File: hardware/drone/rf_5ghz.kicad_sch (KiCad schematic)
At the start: 19 parts, among them J5 Conn_01x06_Pin, U7 CC3350, U8 DPX167125DT-8197B1, U9 DEA162450BT-1295A1, Y1 Crystal_GND24

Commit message: Small cleanup
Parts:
- added R35, R36, R37, R38, R39: R, symbol Device:R
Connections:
- net CC_SDMMC1_CMD: now also R35.2
- net CC_SDMMC1_D0: now also R36.2
- net CC_SDMMC1_D1: now also R37.2
- net CC_SDMMC1_D2: now also R38.2
- net CC_SDMMC1_D3: now also R39.2
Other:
- moved on the sheet: C43, C44, Y1

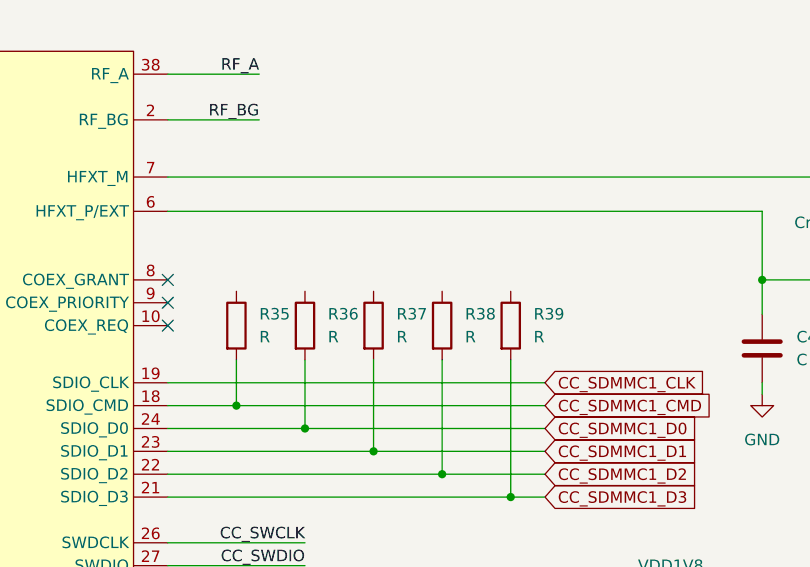
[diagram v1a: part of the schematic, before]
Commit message: Small cleanup and pinmuxxed OSPI_NRESET
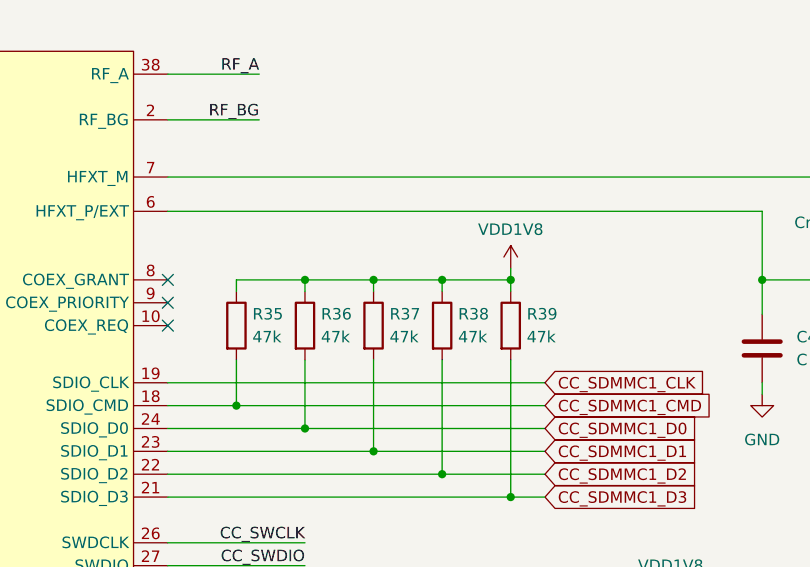
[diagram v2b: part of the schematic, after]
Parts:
- R35, R36, R37, R38, R39: value R -> 47k
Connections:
- net VDD1V8: now also R35.1, R36.1, R37.1, R38.1, R39.1
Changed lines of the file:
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@@
 	)
 	(junction
+		(at 166.37 62.23)
+		(diameter 0)
+		(color 0 0 0 0)
+	)
+	(junction
 		(at 53.34 165.1)
 		(diameter 0)
@@
 	)
 	(junction
+		(at 173.99 62.23)
+		(diameter 0)
+		(color 0 0 0 0)
+	)
+	(junction
+		(at 181.61 62.23)
+		(diameter 0)
+		(color 0 0 0 0)
+	)
+	(junction
+		(at 189.23 62.23)
+		(diameter 0)
+		(color 0 0 0 0)
+	)
+	(junction
 		(at 77.47 39.37)
 		(diameter 0)
@@
 	(wire
 		(pts
+			(xy 173.99 62.23) (xy 173.99 63.5)
+		)
+		(stroke
+			(width 0)
+			(type default)
+		)
+	)
+	(wire
+		(pts
 			(xy 62.23 74.93) (xy 62.23 76.2)
 		)
@@
 	(wire
 		(pts
+			(xy 189.23 62.23) (xy 189.23 60.96)
+		)
+		(stroke
+			(width 0)
+			(type default)
+		)
+	)
+	(wire
+		(pts
+			(xy 189.23 62.23) (xy 189.23 63.5)
+		)
+		(stroke
+			(width 0)
+			(type default)
+		)
+	)
+	(wire
+		(pts
 			(xy 207.01 99.06) (xy 207.01 101.6)
 		)
@@
 	(wire
 		(pts
+			(xy 173.99 62.23) (xy 181.61 62.23)
+		)
+		(stroke
+			(width 0)
+			(type default)
+		)
+	)
+	(wire
+		(pts
+			(xy 158.75 62.23) (xy 166.37 62.23)
+		)
+		(stroke
+			(width 0)
+			(type default)
+		)
+	)
+	(wire
+		(pts
 			(xy 90.17 64.77) (xy 81.28 64.77)
 		)
@@
 	(wire
 		(pts
+			(xy 181.61 62.23) (xy 189.23 62.23)
+		)
+		(stroke
+			(width 0)
+			(type default)
+		)
+	)
+	(wire
+		(pts
 			(xy 110.49 165.1) (xy 114.3 165.1)
 		)
@@
 	(wire
 		(pts
+			(xy 158.75 63.5) (xy 158.75 62.23)
+		)
+		(stroke
+			(width 0)
+			(type default)
+		)
+	)
+	(wire
+		(pts
 			(xy 151.13 86.36) (xy 189.23 86.36)
 		)
@@
 	(wire
 		(pts
+			(xy 166.37 62.23) (xy 173.99 62.23)
+		)
+		(stroke
+			(width 0)
+			(type default)
+		)
+	)
+	(wire
+		(pts
 			(xy 86.36 139.7) (xy 88.9 139.7)
 		)
@@
 	(wire
 		(pts
+			(xy 181.61 62.23) (xy 181.61 63.5)
+		)
+		(stroke
+			(width 0)
+			(type default)
+		)
+	)
+	(wire
+		(pts
 			(xy 237.49 73.66) (xy 237.49 74.93)
 		)
@@
 	(wire
 		(pts
+			(xy 166.37 62.23) (xy 166.37 63.5)
+		)
+		(stroke
+			(width 0)
+			(type default)
+		)
+	)
+	(wire
+		(pts
 			(xy 196.85 106.68) (xy 209.55 106.68)
 		)
@@
 		(in_pos_files yes)
 		(dnp no)
-		(fields_autoplaced yes)
 		(property "Reference" "R35"
-			(at 161.29 66.0399 0)
+			(at 160.528 66.04 0)
 			(show_name no)
 			(do_not_autoplace no)
@@
 			)
 		)
-		(property "Value" "R"
-			(at 161.29 68.5799 0)
+		(property "Value" "47k"
+			(at 160.528 68.58 0)
 			(show_name no)
 			(do_not_autoplace no)
@@
 		(in_pos_files yes)
 		(dnp no)
-		(fields_autoplaced yes)
 		(property "Reference" "R38"
-			(at 184.15 66.0399 0)
+			(at 183.388 66.04 0)
 			(show_name no)
 			(do_not_autoplace no)
@@
 			)
 		)
-		(property "Value" "R"
-			(at 184.15 68.5799 0)
+		(property "Value" "47k"
+			(at 183.388 68.58 0)
 			(show_name no)
 			(do_not_autoplace no)
@@
 		(in_pos_files yes)
 		(dnp no)
-		(fields_autoplaced yes)
 		(property "Reference" "R36"
-			(at 168.91 66.0399 0)
+			(at 168.148 66.04 0)
 			(show_name no)
 			(do_not_autoplace no)
@@
 			)
 		)
-		(property "Value" "R"
-			(at 168.91 68.5799 0)
+		(property "Value" "47k"
+			(at 168.148 68.58 0)
 			(show_name no)
 			(do_not_autoplace no)
@@
 		(in_pos_files yes)
 		(dnp no)
-		(fields_autoplaced yes)
 		(property "Reference" "R39"
-			(at 191.77 66.0399 0)
+			(at 191.008 66.04 0)
 			(show_name no)
 			(do_not_autoplace no)
@@
 			)
 		)
-		(property "Value" "R"
-			(at 191.77 68.5799 0)
+		(property "Value" "47k"
+			(at 191.008 68.58 0)
 			(show_name no)
 			(do_not_autoplace no)
@@
 	)
 	(symbol
+		(lib_id "power:VDD")
+		(at 189.23 60.96 0)
+		(unit 1)
+		(body_style 1)
+		(exclude_from_sim no)
+		(in_bom yes)
+		(on_board yes)
+		(in_pos_files yes)
+		(dnp no)
+		(property "Reference" "#PWR0196"
+			(at 189.23 64.77 0)
+			(hide yes)
+			(show_name no)
+			(do_not_autoplace no)
+			(effects
+				(font
+					(size 1.27 1.27)
+				)
+			)
+		)
+		(property "Value" "VDD1V8"
+			(at 189.23 56.642 0)
+			(show_name no)
+			(do_not_autoplace no)
+			(effects
+				(font
+					(size 1.27 1.27)
+				)
+			)
+		)
+		(property "Footprint" ""
+			(at 189.23 60.96 0)
+			(hide yes)
+			(show_name no)
+			(do_not_autoplace no)
+			(effects
+				(font
+					(size 1.27 1.27)
+				)
+			)
+		)
+		(property "Datasheet" ""
+			(at 189.23 60.96 0)
+			(hide yes)
+			(show_name no)
+			(do_not_autoplace no)
+			(effects
+				(font
+					(size 1.27 1.27)
+				)
+			)
+		)
+		(property "Description" "Power symbol creates a global label with name \"VDD\""
+			(at 189.23 60.96 0)
+			(hide yes)
+			(show_name no)
+			(do_not_autoplace no)
+			(effects
+				(font
+					(size 1.27 1.27)
+				)
+			)
+		)
+		(pin "1"
+		)
+		(instances
+			(project "drone"
+				(path "/62c402a6-ed3f-446b-8423-821e9cc6908b/5e69e925-338b-411d-9923-3dc150eb85e3"
+					(reference "#PWR0196")
+					(unit 1)
+				)
+			)
+		)
+	)
+	(symbol
 		(lib_id "Device:R")
 		(at 173.99 67.31 0)
@@
 		(in_pos_files yes)
 		(dnp no)
-		(fields_autoplaced yes)
 		(property "Reference" "R37"
-			(at 176.53 66.0399 0)
+			(at 175.768 66.04 0)
 			(show_name no)
 			(do_not_autoplace no)
@@
 			)
 		)
-		(property "Value" "R"
-			(at 176.53 68.5799 0)
+		(property "Value" "47k"
+			(at 175.768 68.58 0)
 			(show_name no)
 			(do_not_autoplace no)

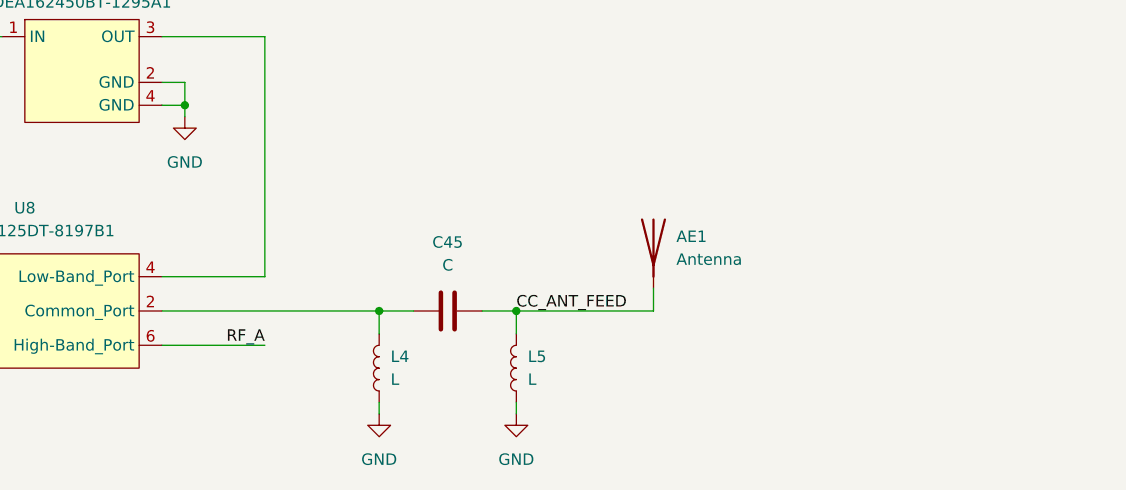
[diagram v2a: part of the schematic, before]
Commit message: Added easier RF tuning setup with MM8030
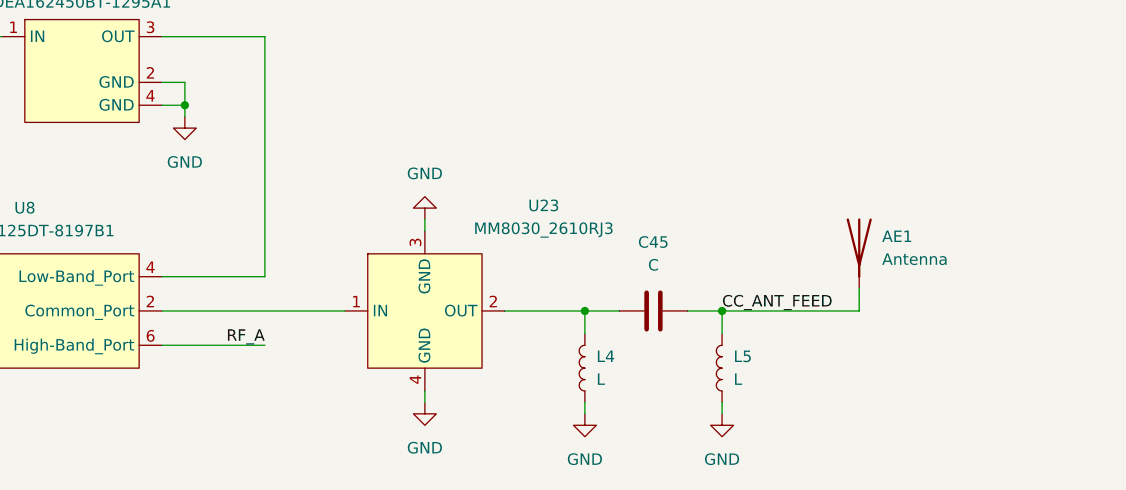
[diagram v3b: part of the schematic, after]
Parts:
- added U23: MM8030_2610RJ3, symbol SoftDrone:MM8030_2610RJ3
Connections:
- net GND: now also U23.3 (GND), U23.4 (GND)
- net at C45.1, L4.2: now also U23.2 (OUT); no longer U8.2 (Common_Port)
- new net: U23.1 (IN), U8.2 (Common_Port)
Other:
- moved on the sheet: AE1, C45, L4, L5

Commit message: Started footprint assignments
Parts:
- J5: footprint RF_Module:Ai-Thinker-Ra-01-LoRa -> (none)
- U7: footprint Display_7Segment:CC56-12GWA -> CC3350ENJARSBR:QFN40P500X500X80-41N-D
- U8: footprint (none) -> DPX167125DT-8197B1:DPX167125DT8197B1
- U9: footprint (none) -> DEA162450BT-1295A1:DEA162450BT1295A1
- Y1: footprint Package_DFN_QFN:DFN-6-1EP_3x2mm_P0.5mm_EP1.65x1.35mm -> (none)
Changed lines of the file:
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@@
 			)
 		)
-		(property "Footprint" ""
+		(property "Footprint" "DEA162450BT-1295A1:DEA162450BT1295A1"
 			(at 77.47 138.43 0)
 			(hide yes)
@@
 			)
 		)
-		(property "Footprint" ""
+		(property "Footprint" "DPX167125DT-8197B1:DPX167125DT8197B1"
 			(at 71.12 165.1 0)
 			(hide yes)
@@
 			)
 		)
-		(property "Footprint" "RF_Module:Ai-Thinker-Ra-01-LoRa"
+		(property "Footprint" ""
 			(at 214.63 106.68 0)
 			(hide yes)
@@
 			)
 		)
-		(property "Footprint" "Display_7Segment:CC56-12GWA"
+		(property "Footprint" "CC3350ENJARSBR:QFN40P500X500X80-41N-D"
 			(at 120.65 73.66 0)
 			(hide yes)
@@
 			)
 		)
-		(property "Footprint" "Package_DFN_QFN:DFN-6-1EP_3x2mm_P0.5mm_EP1.65x1.35mm"
+		(property "Footprint" ""
 			(at 227.33 62.23 0)
 			(hide yes)

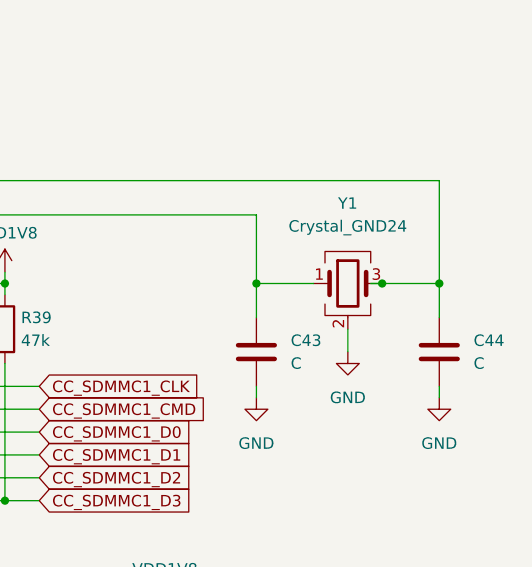
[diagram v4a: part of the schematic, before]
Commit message: Continued footprint assignments
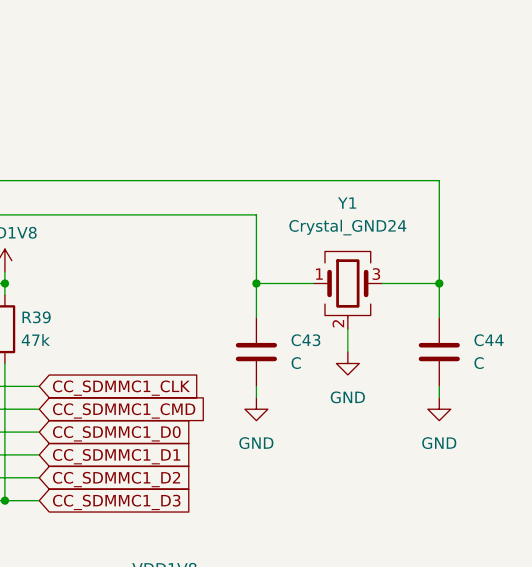
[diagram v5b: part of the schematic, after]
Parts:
- U23: footprint (none) -> SoftDroneLibrary:MM8030-2610RJ3
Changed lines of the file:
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@@
+	)
+	(junction
+		(at 237.49 62.23)
+		(diameter 0)
+		(color 0 0 0 0)
 	)
 	(junction
@@
 	)
 	(junction
-		(at 237.49 62.23)
-		(diameter 0)
-		(color 0 0 0 0)
-	)
-	(junction
 		(at 123.19 115.57)
 		(diameter 0)
@@
 	(junction
 		(at 217.17 62.23)
-		(diameter 0)
-		(color 0 0 0 0)
-	)
-	(junction
-		(at 231.14 62.23)
 		(diameter 0)
 		(color 0 0 0 0)
@@
 	(wire
 		(pts
-			(xy 229.87 62.23) (xy 231.14 62.23)
-		)
-		(stroke
-			(width 0)
-			(type default)
-		)
-	)
-	(wire
-		(pts
 			(xy 87.63 46.99) (xy 87.63 44.45)
 		)
@@
 	(wire
 		(pts
-			(xy 237.49 62.23) (xy 231.14 62.23)
-		)
-		(stroke
-			(width 0)
-			(type default)
-		)
-	)
-	(wire
-		(pts
 			(xy 90.17 57.15) (xy 87.63 57.15)
 		)
@@
 	(wire
 		(pts
+			(xy 231.14 62.23) (xy 237.49 62.23)
+		)
+		(stroke
+			(width 0)
+			(type default)
+		)
+	)
+	(wire
+		(pts
 			(xy 148.59 165.1) (xy 163.83 165.1)
 		)
@@
 	(wire
 		(pts
+			(xy 133.35 165.1) (xy 133.35 167.64)
+		)
+		(stroke
+			(width 0)
+			(type default)
+		)
+	)
+	(wire
+		(pts
+			(xy 166.37 62.23) (xy 166.37 63.5)
+		)
+		(stroke
+			(width 0)
+			(type default)
+		)
+	)
+	(wire
+		(pts
+			(xy 196.85 106.68) (xy 209.55 106.68)
+		)
+		(stroke
+			(width 0)
+			(type default)
+		)
+	)
+	(wire
+		(pts
+			(xy 31.75 48.26) (xy 31.75 49.53)
+		)
+		(stroke
+			(width 0)
+			(type default)
+		)
+	)
+	(wire
+		(pts
+			(xy 86.36 165.1) (xy 106.68 165.1)
+		)
+		(stroke
+			(width 0)
+			(type default)
+		)
+	)
+	(wire
+		(pts
+			(xy 40.64 62.23) (xy 81.28 62.23)
+		)
+		(stroke
+			(width 0)
+			(type default)
+		)
+	)
+	(wire
+		(pts
+			(xy 97.79 161.29) (xy 86.36 161.29)
+		)
+		(stroke
+			(width 0)
+			(type default)
+		)
+	)
+	(wire
+		(pts
+			(xy 148.59 165.1) (xy 144.78 165.1)
+		)
+		(stroke
+			(width 0)
+			(type default)
+		)
+	)
+	(wire
+		(pts
 			(xy 237.49 62.23) (xy 237.49 66.04)
-		)
-		(stroke
-			(width 0)
-			(type default)
-		)
-	)
-	(wire
-		(pts
-			(xy 133.35 165.1) (xy 133.35 167.64)
-		)
-		(stroke
-			(width 0)
-			(type default)
-		)
-	)
-	(wire
-		(pts
-			(xy 166.37 62.23) (xy 166.37 63.5)
-		)
-		(stroke
-			(width 0)
-			(type default)
-		)
-	)
-	(wire
-		(pts
-			(xy 196.85 106.68) (xy 209.55 106.68)
-		)
-		(stroke
-			(width 0)
-			(type default)
-		)
-	)
-	(wire
-		(pts
-			(xy 31.75 48.26) (xy 31.75 49.53)
-		)
-		(stroke
-			(width 0)
-			(type default)
-		)
-	)
-	(wire
-		(pts
-			(xy 86.36 165.1) (xy 106.68 165.1)
-		)
-		(stroke
-			(width 0)
-			(type default)
-		)
-	)
-	(wire
-		(pts
-			(xy 40.64 62.23) (xy 81.28 62.23)
-		)
-		(stroke
-			(width 0)
-			(type default)
-		)
-	)
-	(wire
-		(pts
-			(xy 97.79 161.29) (xy 86.36 161.29)
-		)
-		(stroke
-			(width 0)
-			(type default)
-		)
-	)
-	(wire
-		(pts
-			(xy 148.59 165.1) (xy 144.78 165.1)
 		)
 		(stroke
@@
 			)
 		)
-		(property "Footprint" ""
+		(property "Footprint" "SoftDroneLibrary:MM8030-2610RJ3"
 			(at 115.57 165.1 0)
 			(hide yes)

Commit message: More footprints
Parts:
- C35, C36, C37, C38, C39, C40, C41: footprint (none) -> Capacitor_SMD:C_0201_0603Metric
- C42: footprint (none) -> Capacitor_SMD:C_0402_1005Metric
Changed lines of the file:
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@@
 			)
 		)
-		(property "Footprint" ""
+		(property "Footprint" "Capacitor_SMD:C_0201_0603Metric"
 			(at 67.0052 48.26 0)
 			(hide yes)
@@
 			)
 		)
-		(property "Footprint" ""
+		(property "Footprint" "Capacitor_SMD:C_0201_0603Metric"
 			(at 51.7652 78.74 0)
 			(hide yes)
@@
 			)
 		)
-		(property "Footprint" ""
+		(property "Footprint" "Capacitor_SMD:C_0201_0603Metric"
 			(at 41.6052 71.12 0)
 			(hide yes)
@@
 			)
 		)
-		(property "Footprint" ""
+		(property "Footprint" "Capacitor_SMD:C_0201_0603Metric"
 			(at 78.4352 48.26 0)
 			(hide yes)
@@
 			)
 		)
-		(property "Footprint" ""
+		(property "Footprint" "Capacitor_SMD:C_0201_0603Metric"
 			(at 55.5752 48.26 0)
 			(hide yes)
@@
 			)
 		)
-		(property "Footprint" ""
+		(property "Footprint" "Capacitor_SMD:C_0201_0603Metric"
 			(at 44.1452 48.26 0)
 			(hide yes)
@@
 			)
 		)
-		(property "Footprint" ""
+		(property "Footprint" "Capacitor_SMD:C_0201_0603Metric"
 			(at 32.7152 48.26 0)
 			(hide yes)
@@
 			)
 		)
-		(property "Footprint" ""
+		(property "Footprint" "Capacitor_SMD:C_0402_1005Metric"
 			(at 63.1952 83.82 0)
 			(hide yes)

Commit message: More footprints
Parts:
- C45: footprint (none) -> Capacitor_SMD:C_0402_1005Metric
- J5: footprint (none) -> Connector_PinHeader_2.54mm:PinHeader_1x06_P2.54mm_Vertical
- L4, L5: footprint (none) -> Inductor_SMD:L_0402_1005Metric
- R35, R36, R37, R38, R39: footprint (none) -> Resistor_SMD:R_0402_1005Metric
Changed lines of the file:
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@@
 			)
 		)
-		(property "Footprint" ""
+		(property "Footprint" "Capacitor_SMD:C_0402_1005Metric"
 			(at 144.78 164.1348 0)
 			(hide yes)
@@
 			)
 		)
-		(property "Footprint" ""
+		(property "Footprint" "Resistor_SMD:R_0402_1005Metric"
 			(at 156.972 67.31 90)
 			(hide yes)
@@
 			)
 		)
-		(property "Footprint" ""
+		(property "Footprint" "Connector_PinHeader_2.54mm:PinHeader_1x06_P2.54mm_Vertical"
 			(at 214.63 106.68 0)
 			(hide yes)
@@
 			)
 		)
-		(property "Footprint" ""
+		(property "Footprint" "Inductor_SMD:L_0402_1005Metric"
 			(at 148.59 171.45 0)
 			(hide yes)
@@
 			)
 		)
-		(property "Footprint" ""
+		(property "Footprint" "Resistor_SMD:R_0402_1005Metric"
 			(at 179.832 67.31 90)
 			(hide yes)
@@
 			)
 		)
-		(property "Footprint" ""
+		(property "Footprint" "Inductor_SMD:L_0402_1005Metric"
 			(at 133.35 171.45 0)
 			(hide yes)
@@
 			)
 		)
-		(property "Footprint" ""
+		(property "Footprint" "Resistor_SMD:R_0402_1005Metric"
 			(at 164.592 67.31 90)
 			(hide yes)
@@
 			)
 		)
-		(property "Footprint" ""
+		(property "Footprint" "Resistor_SMD:R_0402_1005Metric"
 			(at 187.452 67.31 90)
 			(hide yes)
@@
 			)
 		)
-		(property "Footprint" ""
+		(property "Footprint" "Resistor_SMD:R_0402_1005Metric"
 			(at 172.212 67.31 90)
 			(hide yes)

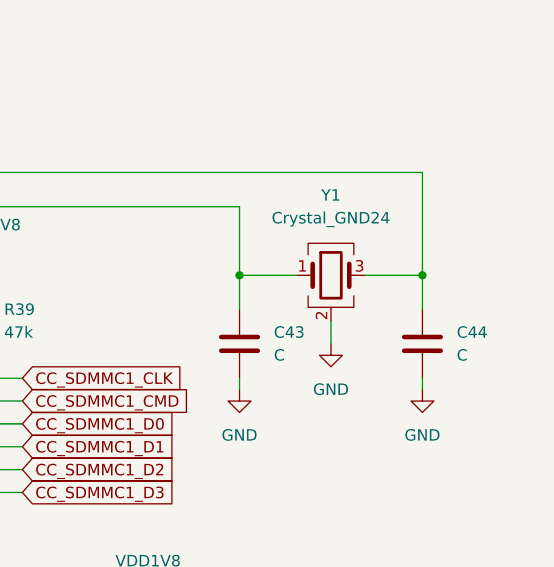
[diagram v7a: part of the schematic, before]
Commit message: Completed footprint assignments
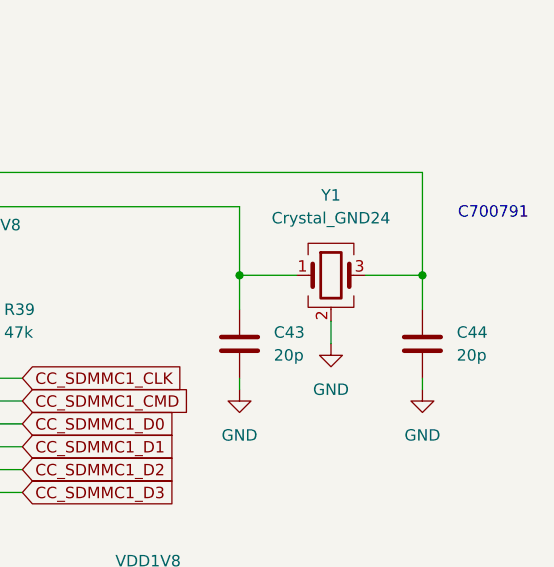
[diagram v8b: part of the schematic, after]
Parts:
- C43, C44: value C -> 20p; footprint (none) -> Capacitor_SMD:C_0201_0603Metric
- Y1: footprint (none) -> Crystal:Crystal_SMD_3225-4Pin_3.2x2.5mm
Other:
- note added: "C700791"
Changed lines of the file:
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@@
 		)
 	)
+	(text "C700791"
+		(exclude_from_sim no)
+		(at 245.364 55.372 0)
+		(effects
+			(font
+				(size 1.27 1.27)
+			)
+		)
+	)
 	(junction
 		(at 118.11 115.57)
@@
 			)
 		)
-		(property "Value" "C"
+		(property "Value" "20p"
 			(at 220.98 71.1199 0)
 			(show_name no)
@@
 			)
 		)
-		(property "Footprint" ""
+		(property "Footprint" "Capacitor_SMD:C_0201_0603Metric"
 			(at 218.1352 73.66 0)
 			(hide yes)
@@
 			)
 		)
-		(property "Value" "C"
+		(property "Value" "20p"
 			(at 241.3 71.1199 0)
 			(show_name no)
@@
 			)
 		)
-		(property "Footprint" ""
+		(property "Footprint" "Capacitor_SMD:C_0201_0603Metric"
 			(at 238.4552 73.66 0)
 			(hide yes)
@@
 			)
 		)
-		(property "Footprint" ""
+		(property "Footprint" "Crystal:Crystal_SMD_3225-4Pin_3.2x2.5mm"
 			(at 227.33 62.23 0)
 			(hide yes)
